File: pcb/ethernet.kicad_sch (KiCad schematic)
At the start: 1 part, among them U11 ENC28J60x-SP

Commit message: WIP schematic
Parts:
- renumbered U11 to U51
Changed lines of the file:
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@@
 		(dnp no)
 		(fields_autoplaced yes)
-		(property "Reference" "U11"
+		(property "Reference" "U51"
 			(at 134.2741 71.12 0)
 			(effects
@@
 			(project ""
 				(path "/e63e39d7-6ac0-4ffd-8aa3-1841a4541b55/5f1e9cad-1441-4289-92fe-31e435d6f32d"
-					(reference "U11")
+					(reference "U51")
 					(unit 1)
 				)

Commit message: WIP PCB
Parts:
- renumbered U51 to U?
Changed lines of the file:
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@@
 		(shape input)
 		(at 111.76 83.82 180)
-		(fields_autoplaced yes)
 		(effects
 			(font
@@
 		(shape input)
 		(at 111.76 78.74 180)
-		(fields_autoplaced yes)
 		(effects
 			(font
@@
 		(shape output)
 		(at 111.76 96.52 180)
-		(fields_autoplaced yes)
 		(effects
 			(font
@@
 		(shape input)
 		(at 111.76 91.44 180)
-		(fields_autoplaced yes)
 		(effects
 			(font
@@
 		(shape input)
 		(at 111.76 88.9 180)
-		(fields_autoplaced yes)
 		(effects
 			(font
@@
 		(shape output)
 		(at 111.76 86.36 180)
-		(fields_autoplaced yes)
 		(effects
 			(font
@@
 		(dnp no)
 		(fields_autoplaced yes)
-		(property "Reference" "U51"
+		(property "Reference" "U?"
 			(at 134.2741 71.12 0)
 			(effects
@@
 			(project ""
 				(path "/e63e39d7-6ac0-4ffd-8aa3-1841a4541b55/5f1e9cad-1441-4289-92fe-31e435d6f32d"
-					(reference "U51")
+					(reference "U?")
 					(unit 1)
 				)

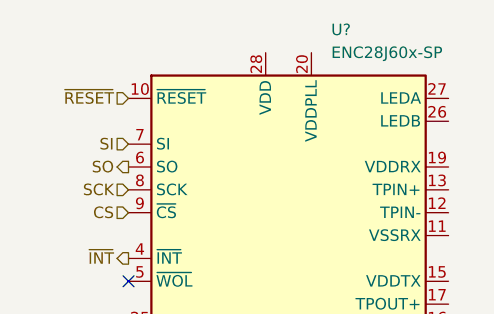
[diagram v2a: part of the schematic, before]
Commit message: PCB: add reset circuit, xtal
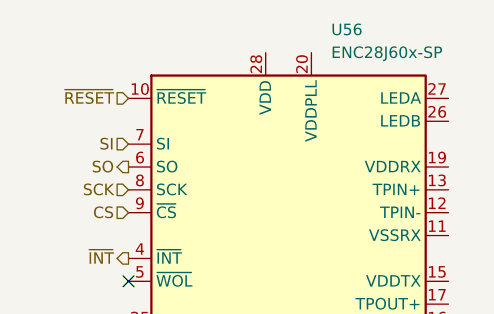
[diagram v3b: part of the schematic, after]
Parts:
- gave numbers to parts that had none: 1
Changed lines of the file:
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@@
 (kicad_sch
-	(version 20231120)
+	(version 20250114)
 	(generator "eeschema")
-	(generator_version "8.0")
+	(generator_version "9.0")
 	(paper "A4")
 	(no_connect
@@
 		(dnp no)
 		(fields_autoplaced yes)
-		(property "Reference" "U?"
+		(property "Reference" "U56"
 			(at 134.2741 71.12 0)
 			(effects
@@
 			(project ""
 				(path "/e63e39d7-6ac0-4ffd-8aa3-1841a4541b55/5f1e9cad-1441-4289-92fe-31e435d6f32d"
-					(reference "U?")
+					(reference "U56")
 					(unit 1)
 				)

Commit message: WIP schematic
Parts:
- renumbered U56 to U57
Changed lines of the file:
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@@
 		(dnp no)
 		(fields_autoplaced yes)
-		(property "Reference" "U56"
+		(property "Reference" "U57"
 			(at 134.2741 71.12 0)
 			(effects
@@
 			(project ""
 				(path "/e63e39d7-6ac0-4ffd-8aa3-1841a4541b55/5f1e9cad-1441-4289-92fe-31e435d6f32d"
-					(reference "U56")
+					(reference "U57")
 					(unit 1)
 				)

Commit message: WIP schematic
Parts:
- added C10, C9: 22pF, symbol Device:C_Small
- added C11, C12, C13, C14, C16, C17: 0.1µF, symbol Device:C
- added C15: 10µF, symbol Device:C_Polarized
- added FB1: FerriteBead_Small, symbol Device:FerriteBead_Small
- added J6: Conn_01x01_Pin, symbol Connector:Conn_01x01_Pin
- added J7: ARJM11A3-009-AB-ER2-T, Connector_RJ:RJ45_Amphenol_RJMG1BD3B8K1ANR, symbol Connector:RJ45_Amphenol_RJMG1BD3B8K1ANR
- added R17: 2.32kΩ 1%, symbol Device:R
- added R18, R19, R20, R21: 49.9Ω 1%, symbol Device:R_Small
- added R22, R23: 220Ω, symbol Device:R
- added U1: 74HCT125, symbol 74xx:74LS125
- added Y2: 25MHz, symbol Device:Crystal
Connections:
- net SI: now also U1.1
- net SO: now also U1.3; no longer U57.6 (SO)
- net ~{INT}: now also U1.6; no longer U57.4 (~{INT})
- net at U57.1 (VCAP): now also C15.1
- net GND: now reaches U57.11 (VSSRX)
- net GND: now also U57.18 (VSSTX), U57.2 (VSS), U57.21 (VSSPLL), U57.22 (VSSOSC), C10.1, C11.2, C12.2, C13.2, C14.2, C15.2, C16.2, C17.2, C9.1, J7.R8, R17.1, U1.4
- net at U57.12 (TPIN-): now also J7.R6 (RD-), R19.2
- net at U57.13 (TPIN+): now also J7.R3 (RD+), R18.1
- net at U57.14 (RBIAS): now also R17.2
- net +3.3V: now reaches U57.15 (VDDTX)
- net +3.3V: now also U57.19 (VDDRX), U57.20 (VDDPLL), U57.25 (VDDOSC), U57.28 (VDD), C11.1, C12.1, C13.1, C14.1, FB1.1, J7.L1, J7.L4
- net at U57.16 (TPOUT-): now also J7.R2 (TD-), R21.2
- net at U57.17 (TPOUT+): now also J7.R1 (TD+), R20.1
- net at U57.23 (OSC1): now also C9.2, Y2.2
- net at U57.24 (OSC2): now also C10.2, Y2.1
- net LEDB: now reaches U57.26 (LEDB)
- net LEDB: now also R23.2
- net LEDA: now reaches U57.27 (LEDA)
- net LEDA: now also R22.2
- new net: C16.1, FB1.2, J7.R4 (TCT), R20.2, R21.1
- new net: U1.5, U57.4 (~{INT})
- new net: C17.1, R18.2, R19.1
- new net: J6.1 (Pin_1), J7.SH
- new net: J7.L3, R22.1
- new net: J7.L2, R23.1
- new net: U1.2, U57.6 (SO)
- no-connect marks 1 -> 3
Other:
- moved on the sheet: U57

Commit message: WIP schematic
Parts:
- renumbered C9 to C14, C10 to C15, C11 to C16, C12 to C17, C13 to C18, C14 to C19, C15 to C20, C16 to C21, C17 to C22, J6 to J7, J7 to J8

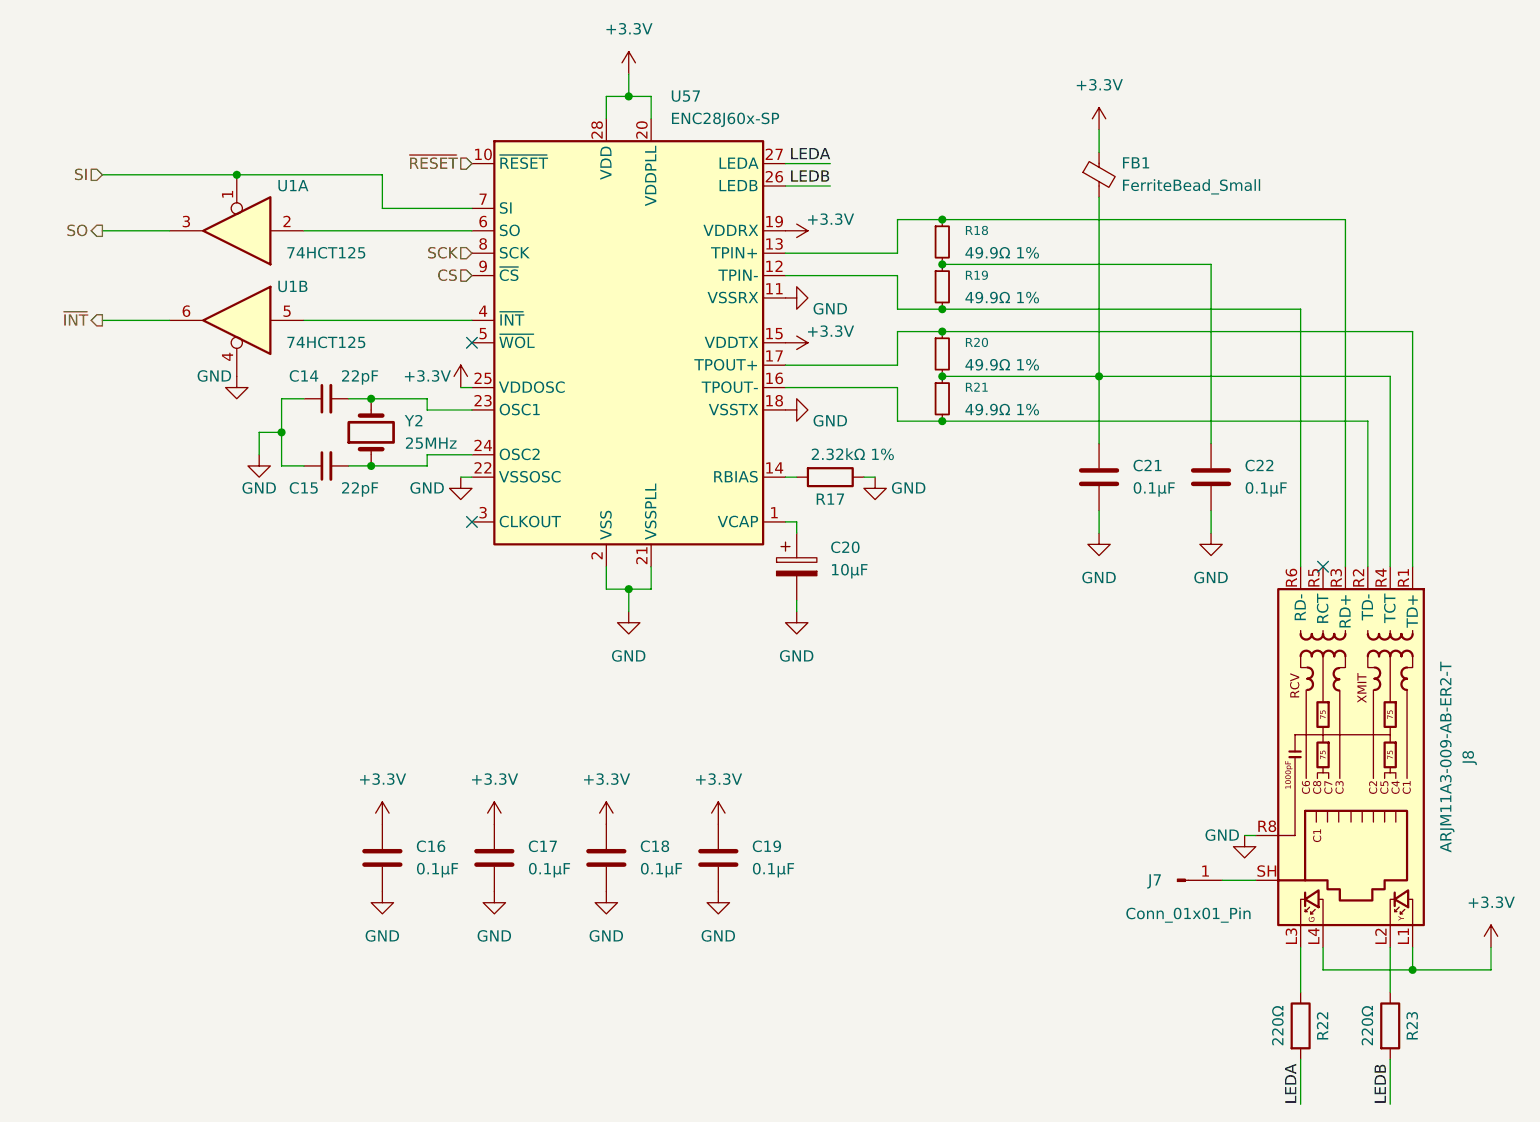
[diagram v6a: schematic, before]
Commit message: WIP PCB (add bypass caps, minor fixes)
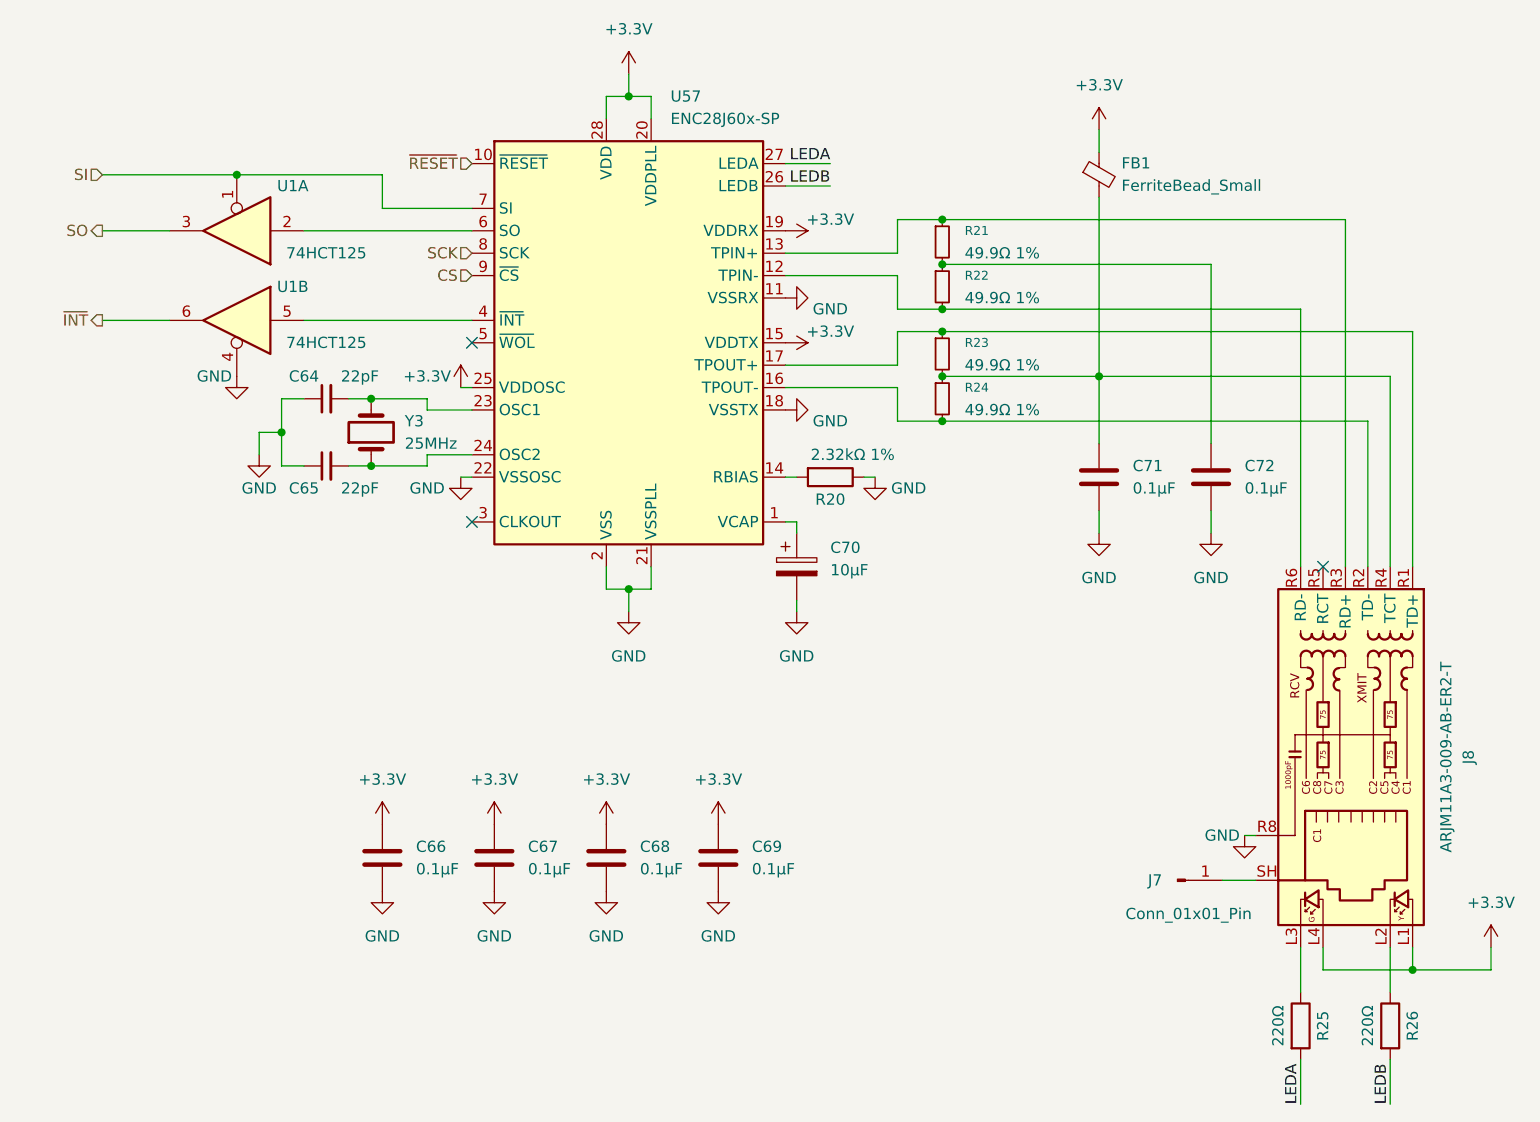
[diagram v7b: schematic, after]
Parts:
- renumbered C14 to C64, C15 to C65, C16 to C66, C17 to C67, C18 to C68, C19 to C69, C20 to C70, C21 to C71, C22 to C72, R17 to R20, R18 to R21, R19 to R22, R20 to R23, R21 to R24, R22 to R25, R23 to R26, Y2 to Y3
